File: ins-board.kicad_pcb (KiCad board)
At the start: 4 copper layers, 50 x 23 mm, 93 parts, among them P1 POWER, Q1 FDN306P, Q2 FDC638APZ, U1 24LC128, U10 HMC5883L, U11 H3LIS331DL, U2 STM32F415RGT6, U3 LTC4412, U4 MAX3051, U5 LT1965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

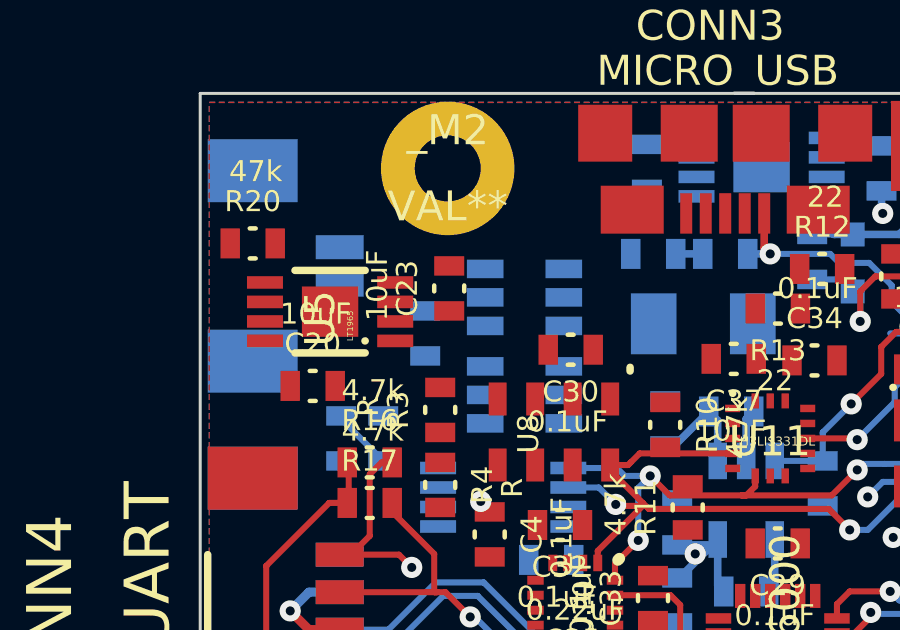
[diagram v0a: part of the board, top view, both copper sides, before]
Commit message: solid copper connection for mounting holes
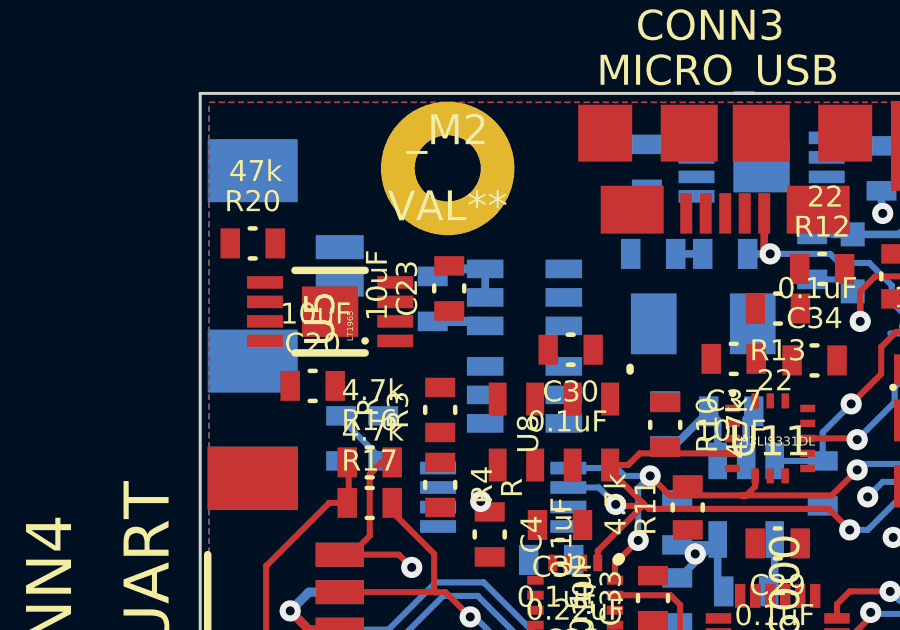
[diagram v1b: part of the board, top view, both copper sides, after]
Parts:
- moved C17 1.18 mm to (39.8, 32.9)
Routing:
- net GND: track 56.4 -> 59.2 mm
- net /V_DC: track 0.00 -> 1.81 mm
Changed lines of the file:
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@@
   (general
     (links 269)
-    (no_connects 89)
+    (no_connects 87)
     (area 16.4 15.14 86.7782 50.939311)
     (thickness 1.6)
     (drawings 6)
-    (tracks 810)
+    (tracks 815)
     (zones 0)
     (modules 93)
@@
   )
   (setup
-    (last_trace_width 0.254)
+    (last_trace_width 0.3048)
     (user_trace_width 0.2032)
     (user_trace_width 0.254)
@@
       (layers *.Cu *.Mask F.SilkS)
       (net 52 GND)
+      (zone_connect 2)
     )
   )
@@
       (layers *.Cu *.Mask F.SilkS)
       (net 52 GND)
+      (zone_connect 2)
     )
   )
@@
       (layers *.Cu *.Mask F.SilkS)
       (net 52 GND)
+      (zone_connect 2)
     )
   )
@@
       (layers *.Cu *.Mask F.SilkS)
       (net 52 GND)
+      (zone_connect 2)
     )
   )
@@
   )
   (module _0603-W (layer B.Cu)
-    (at 39.5 34 90)
+    (at 39.75 32.85 90)
     (fp_text reference C17 (at 0 1.4 90) (layer B.SilkS)
       (effects (font (size 0.7 0.7) (thickness 0.15)) (justify mirror))
@@
   (segment (start 70 41.45) (end 70 41.2) (width 0.2032) (layer F.Cu) (net 17))
   (segment (start 70.55 42) (end 70 41.45) (width 0.2032) (layer F.Cu) (net 17))
-  (segment (start 52.4 32.2) (end 53.35 32.2) (width 0.2032) (layer B.Cu) (net 18) (status C00000))
-  (segment (start 53.35 32.2) (end 53.75 32.6) (width 0.2032) (layer B.Cu) (net 18) (status C00000))
+  (segment (start 52.4 32.2) (end 53.35 32.2) (width 0.2032) (layer B.Cu) (net 18))
+  (segment (start 53.35 32.2) (end 53.75 32.6) (width 0.2032) (layer B.Cu) (net 18))
   (segment (start 54 33.6) (end 54 32.85) (width 0.2032) (layer B.Cu) (net 18))
   (via (at 54 33.6) (size 0.706) (layers F.Cu B.Cu) (net 18))
@@
   (segment (start 60.9 38.95) (end 55.3 38.95) (width 0.2032) (layer B.Cu) (net 48))
   (segment (start 55.3 38.95) (end 55.25 38.95) (width 0.2032) (layer B.Cu) (net 48))
+  (segment (start 39.75 33.6) (end 41.35 33.6) (width 0.3048) (layer B.Cu) (net 49) (status C00000))
+  (segment (start 41.35 33.6) (end 41.5 33.75) (width 0.3048) (layer B.Cu) (net 49) (status C00000))
   (segment (start 51 31.35) (end 53 31.35) (width 0.2032) (layer B.Cu) (net 51))
   (segment (start 56.525 33.275) (end 56.25 33.55) (width 0.2032) (layer B.Cu) (net 51))
@@
   (segment (start 66.25 38.75) (end 66 39) (width 0.2032) (layer F.Cu) (net 51))
   (segment (start 66.25 38.75) (end 66 39) (width 0.2032) (layer F.Cu) (net 51))
+  (segment (start 41.5 31.85) (end 40 31.85) (width 0.3048) (layer B.Cu) (net 52) (status C00000))
+  (segment (start 40 31.85) (end 39.75 32.1) (width 0.3048) (layer B.Cu) (net 52) (status C00000))
+  (segment (start 41.5 31.85) (end 41.5 32.8) (width 0.254) (layer B.Cu) (net 52))
   (segment (start 54.7116 29.2488) (end 54.7116 29.9616) (width 0.254) (layer B.Cu) (net 52))
   (via (at 54.75 30) (size 0.706) (layers F.Cu B.Cu) (net 52))
@@
   (segment (start 58.55 47.9) (end 58.5 47.9) (width 0.2032) (layer B.Cu) (net 69))
   (segment (start 62.65 45.2) (end 62 45.85) (width 0.2032) (layer B.Cu) (net 69))
-  (segment (start 56.05 31.65) (end 56.05 31.1) (width 0.2032) (layer B.Cu) (net 70) (status 400000))
+  (segment (start 56.05 31.65) (end 56.05 31.1) (width 0.2032) (layer B.Cu) (net 70))
   (via (at 56.1 31.05) (size 0.706) (layers F.Cu B.Cu) (net 70))
   (segment (start 56.05 31.1) (end 56.1 31.05) (width 0.2032) (layer B.Cu) (net 70))
@@
   (segment (start 36.7 36.75) (end 36.7 36.85) (width 0.2032) (layer B.Cu) (net 76))
   (segment (start 36.7 36.85) (end 38.1 38.25) (width 0.2032) (layer B.Cu) (net 76))
-  (segment (start 53.15 30.7) (end 52.4 30.7) (width 0.2032) (layer B.Cu) (net 77) (status 800000))
+  (segment (start 53.15 30.7) (end 52.4 30.7) (width 0.2032) (layer B.Cu) (net 77))
   (segment (start 53.1 30.7) (end 53.15 30.7) (width 0.254) (layer B.Cu) (net 77))
   (segment (start 53.15 30.7) (end 55.3 30.7) (width 0.254) (layer B.Cu) (net 77))

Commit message: power routing
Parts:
- moved R13 2.04 mm to (49.4, 32.5), turned to 90 degrees
- moved C5 1.70 mm to (56.5, 42.6), turned to 90 degrees
- moved R12 1.44 mm to (51.6, 32.8)
- moved C26 0.78 mm to (48.1, 34.1)
- moved C9 0.57 mm to (57.8, 42.6), turned to 90 degrees
- moved R8 0.07 mm to (72.1, 38.9)
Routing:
- net /VCC_IO: track 10.4 -> 93.0 mm, vias 0 -> 5
- net /V_IN: track 0.00 -> 16.7 mm
- net VCC: track 37.5 -> 53.7 mm
- net /USB_DP: track 15.8 -> 24.6 mm, vias 1 -> 2
- net /Sensors/I2C_SDA: track 27.8 -> 32.1 mm, vias 4 -> 5
- net /USB_DM: track 19.1 -> 22.3 mm, vias 1 -> 2
- net N-0000043: track 0.00 -> 3.04 mm
- net GND: track 59.2 -> 61.5 mm
- net N-0000044: track 0.00 -> 1.76 mm
- net (no net): track 0.00 -> 0.94 mm, vias 0 -> 1

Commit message: power routing
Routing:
- net VCC: track 53.7 -> 77.8 mm, vias 7 -> 9
- net /VCC_IO: track 93.0 -> 94.9 mm
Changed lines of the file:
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@@
   (general
     (links 269)
-    (no_connects 65)
+    (no_connects 64)
     (area 16.4 15.14 86.7782 50.939311)
     (thickness 1.6)
     (drawings 6)
-    (tracks 919)
+    (tracks 934)
     (zones 0)
     (modules 93)
@@
   )
   (setup
-    (last_trace_width 0.3556)
+    (last_trace_width 0.508)
     (user_trace_width 0.2032)
     (user_trace_width 0.254)
@@
   (segment (start 55.2 34.4) (end 54.9 34.4) (width 0.2032) (layer B.Cu) (net 46))
   (segment (start 49.9 33.75) (end 49.35 33.2) (width 0.2032) (layer F.Cu) (net 46))
+  (segment (start 40.3 33.25) (end 39.95 33.6) (width 0.508) (layer F.Cu) (net 47) (status 400000))
+  (segment (start 39.95 33.6) (end 38.5 33.6) (width 0.508) (layer F.Cu) (net 47) (status 800000))
   (segment (start 36.65 45.125) (end 35.075 45.125) (width 0.508) (layer F.Cu) (net 47))
   (segment (start 34.1 41.9) (end 34.9 41.1) (width 0.508) (layer F.Cu) (net 47))
@@
   (segment (start 58.55 47.9) (end 58.5 47.9) (width 0.2032) (layer B.Cu) (net 69))
   (segment (start 62.65 45.2) (end 62 45.85) (width 0.2032) (layer B.Cu) (net 69))
+  (segment (start 57.95 30) (end 57.95 30.9) (width 0.254) (layer B.Cu) (net 70))
+  (segment (start 57.5 31.35) (end 56.8 31.35) (width 0.254) (layer F.Cu) (net 70) (status 800000))
+  (via (at 57.5 31.35) (size 0.706) (layers F.Cu B.Cu) (net 70))
+  (segment (start 57.95 30.9) (end 57.5 31.35) (width 0.254) (layer B.Cu) (net 70))
+  (segment (start 57.95 30) (end 57.95 29.25) (width 0.254) (layer B.Cu) (net 70))
   (segment (start 56.05 31.65) (end 56.05 31.1) (width 0.2032) (layer B.Cu) (net 70))
   (via (at 56.1 31.05) (size 0.706) (layers F.Cu B.Cu) (net 70))
   (segment (start 56.05 31.1) (end 56.1 31.05) (width 0.2032) (layer B.Cu) (net 70))
-  (segment (start 57.2 30) (end 57.2 30.35) (width 0.254) (layer B.Cu) (net 70))
-  (segment (start 56.8 31.35) (end 56.8 30.8) (width 0.3048) (layer F.Cu) (net 70))
-  (segment (start 57 30.6) (end 56.8 30.8) (width 0.3048) (layer F.Cu) (net 70))
   (segment (start 63.2 29.4) (end 62.9 29.1) (width 0.254) (layer B.Cu) (net 70))
-  (segment (start 62.9 29.1) (end 58.1 29.1) (width 0.254) (layer B.Cu) (net 70))
-  (segment (start 58.1 29.1) (end 57.2 30) (width 0.254) (layer B.Cu) (net 70))
   (segment (start 63.2 29.4) (end 63.2 30.4) (width 0.254) (layer B.Cu) (net 70))
-  (segment (start 57 30.55) (end 57 30.6) (width 0.254) (layer F.Cu) (net 70))
-  (segment (start 57.05 30.5) (end 57 30.55) (width 0.254) (layer F.Cu) (net 70))
-  (via (at 57.05 30.5) (size 0.706) (layers F.Cu B.Cu) (net 70))
-  (segment (start 57.2 30.35) (end 57.05 30.5) (width 0.254) (layer B.Cu) (net 70))
+  (segment (start 58.1 29.1) (end 57.95 29.25) (width 0.254) (layer B.Cu) (net 70))
+  (segment (start 62.9 29.1) (end 58.1 29.1) (width 0.254) (layer B.Cu) (net 70))
   (segment (start 56.8 31.35) (end 55.2 31.35) (width 0.3048) (layer F.Cu) (net 70))
   (segment (start 48.2 44.8) (end 49.1 44.8) (width 0.2032) (layer B.Cu) (net 74))
@@
   (segment (start 36.7 36.75) (end 36.7 36.85) (width 0.2032) (layer B.Cu) (net 76))
   (segment (start 36.7 36.85) (end 38.1 38.25) (width 0.2032) (layer B.Cu) (net 76))
+  (segment (start 38.9 36.7) (end 40.45 35.15) (width 0.2032) (layer Inner2.Cu) (net 77))
+  (segment (start 54.95 28.85) (end 56.05 29.95) (width 0.2032) (layer Inner2.Cu) (net 77))
+  (segment (start 54.05 28.85) (end 54.95 28.85) (width 0.2032) (layer Inner2.Cu) (net 77))
+  (segment (start 53.4 29.5) (end 54.05 28.85) (width 0.2032) (layer Inner2.Cu) (net 77))
+  (segment (start 44.95 29.5) (end 53.4 29.5) (width 0.2032) (layer Inner2.Cu) (net 77))
+  (segment (start 40.45 34) (end 44.95 29.5) (width 0.2032) (layer Inner2.Cu) (net 77))
+  (segment (start 40.45 35.15) (end 40.45 34) (width 0.2032) (layer Inner2.Cu) (net 77))
+  (segment (start 38.1 36.75) (end 38.85 36.75) (width 0.2032) (layer B.Cu) (net 77) (status 400000))
+  (segment (start 38.9 36.7) (end 38.9 36.75) (width 0.2032) (layer F.Cu) (net 77))
+  (via (at 38.9 36.7) (size 0.706) (layers F.Cu B.Cu) (net 77))
+  (segment (start 38.85 36.75) (end 38.9 36.7) (width 0.2032) (layer B.Cu) (net 77))
+  (segment (start 56.05 28.65) (end 56.05 29) (width 0.508) (layer B.Cu) (net 77))
+  (via (at 57 29.95) (size 0.706) (layers F.Cu B.Cu) (net 77))
+  (segment (start 56.05 29) (end 57 29.95) (width 0.508) (layer B.Cu) (net 77))
   (segment (start 52.8828 28.1328) (end 54.3276 28.1328) (width 0.3556) (layer B.Cu) (net 77) (status 400000))
   (segment (start 54.3276 28.1328) (end 54.7116 27.7488) (width 0.3556) (layer B.Cu) (net 77) (status 800000))
@@
   (segment (start 54.7116 27.7488) (end 55.4988 27.7488) (width 0.508) (layer B.Cu) (net 77))
   (segment (start 55.4988 27.7488) (end 56.05 28.3) (width 0.508) (layer B.Cu) (net 77))
-  (segment (start 56.05 28.3) (end 56.05 29.95) (width 0.508) (layer B.Cu) (net 77))
+  (segment (start 56.05 28.3) (end 56.05 28.65) (width 0.508) (layer B.Cu) (net 77))
+  (segment (start 56.05 28.65) (end 56.05 29.95) (width 0.508) (layer B.Cu) (net 77))
   (segment (start 73.3 31.85) (end 73.9 32.45) (width 0.2032) (layer F.Cu) (net 77))
   (via (at 74.25 32.45) (size 0.706) (layers F.Cu B.Cu) (net 77))
@@
   (via (at 60.6 34.9) (size 0.706) (layers F.Cu B.Cu) (net 77))
   (segment (start 56.05 29.95) (end 56.3 29.7) (width 0.2032) (layer F.Cu) (net 77))
-  (via (at 56.05 29.95) (size 0.706) (layers F.Cu B.Cu) (net 77))
-  (segment (start 58.625 30.225) (end 58.625 30.65) (width 0.2032) (layer F.Cu) (net 77))
-  (segment (start 58.1 29.7) (end 58.625 30.225) (width 0.2032) (layer F.Cu) (net 77))
   (segment (start 56.3 29.7) (end 58.1 29.7) (width 0.2032) (layer F.Cu) (net 77))
+  (segment (start 58.1 29.7) (end 58.625 30.225) (width 0.2032) (layer F.Cu) (net 77))
+  (segment (start 58.625 30.225) (end 58.625 30.65) (width 0.2032) (layer F.Cu) (net 77))
+  (via (at 56.05 29.95) (size 0.706) (layers F.Cu B.Cu) (net 77))
   (segment (start 56.5 43.4) (end 57.1 44) (width 0.254) (layer F.Cu) (net 77))
   (via (at 57.1 44.55) (size 0.706) (layers F.Cu B.Cu) (net 77))
@@
   (segment (start 53.1 30.7) (end 53.15 30.7) (width 0.254) (layer B.Cu) (net 77))
   (segment (start 53.15 30.7) (end 55.3 30.7) (width 0.254) (layer B.Cu) (net 77))
+  (segment (start 55.3 30.7) (end 56.05 29.95) (width 0.254) (layer B.Cu) (net 77))
   (segment (start 55.4988 27.7488) (end 56.05 28.3) (width 0.3048) (layer B.Cu) (net 77))
   (segment (start 56.05 28.3) (end 56.05 29.95) (width 0.3048) (layer B.Cu) (net 77))
-  (segment (start 55.3 30.7) (end 56.05 29.95) (width 0.254) (layer B.Cu) (net 77))
   (segment (start 63.8 47.35) (end 64.5 48.05) (width 0.2032) (layer B.Cu) (net 77))
   (segment (start 64.5 48.05) (end 66.65 48.05) (width 0.2032) (layer B.Cu) (net 77))

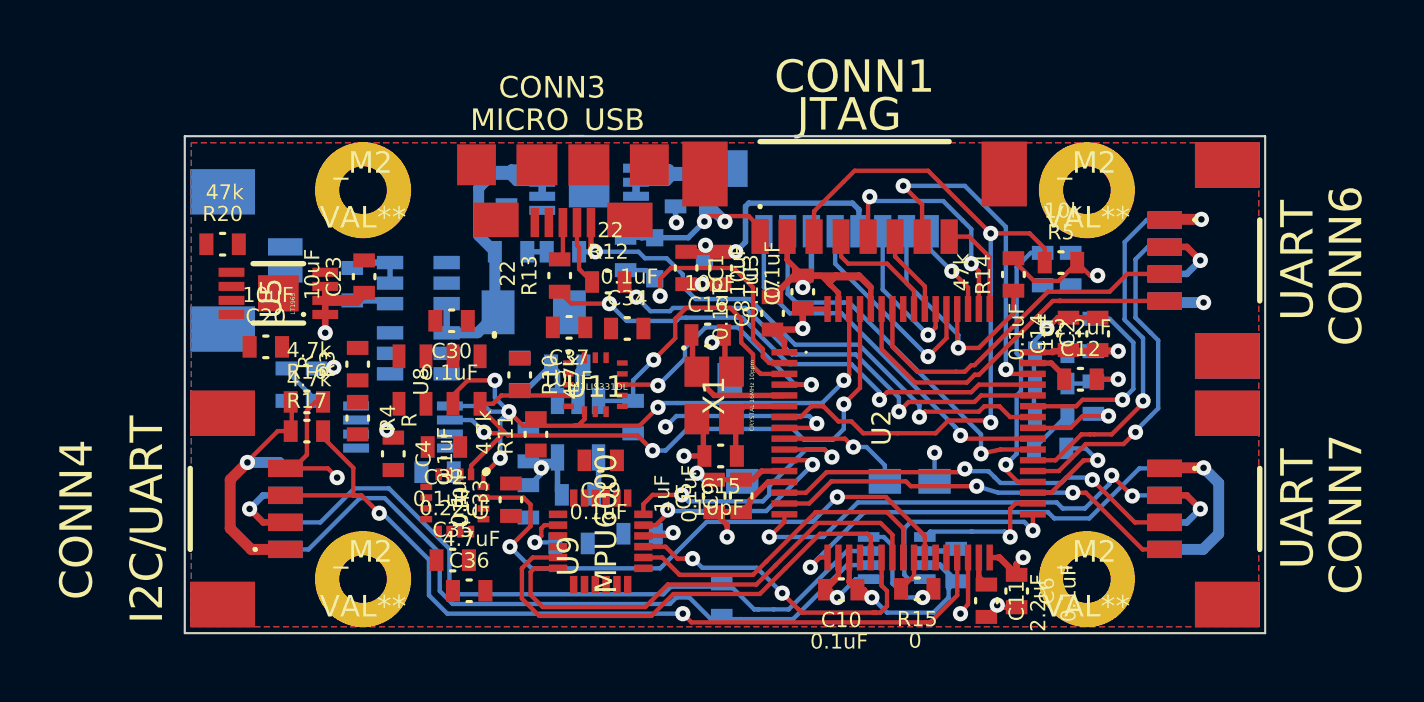
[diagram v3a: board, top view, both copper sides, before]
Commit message: routing, added dimensions
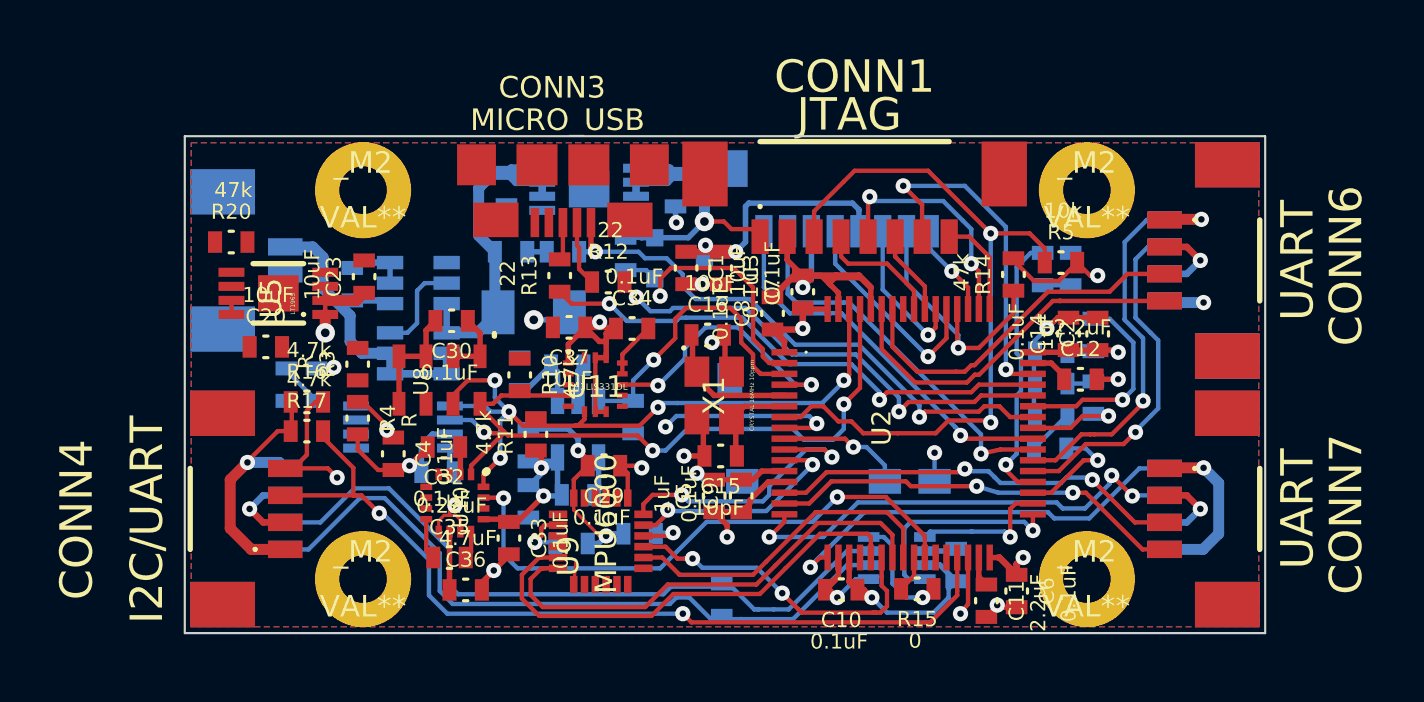
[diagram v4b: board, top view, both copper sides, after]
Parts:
- moved C33 1.78 mm to (47.0, 44.6), turned to 270 degrees
- moved R20 0.41 mm to (34.1, 30.9)
- moved C29 0.29 mm to (51.4, 41.2)
- moved C34 0.22 mm to (52.7, 34.9)
- moved C35 0.19 mm to (44.2, 45.5)
- moved C36 0.17 mm to (45.0, 47.0)
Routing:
- net GND: track 61.5 -> 95.4 mm, vias 13 -> 19
- net /Sensors/VCC_A: track 5.82 -> 30.1 mm, vias 1 -> 4
- net /V_DC: track 1.81 -> 15.4 mm
- net N-0000051: track 0.00 -> 4.45 mm
- net VCC: track 77.8 -> 75.1 mm, vias 9 -> 8
- net N-0000082: track 0.00 -> 2.70 mm
- net /V_BAT_MON_AD: track 36.6 -> 39.0 mm
- net N-0000081: track 0.00 -> 1.91 mm
- net N-0000083: track 0.00 -> 1.30 mm
- net N-0000052: track 0.00 -> 1.30 mm
- net /Sensors/HMC5883L_DRDY: track 27.4 -> 26.4 mm

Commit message: routing (io_en)
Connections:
- U2 pad 28: /IO_EN -> (no net)
- U2 pad 57: (no net) -> /IO_EN
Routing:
- net /IO_EN: track 0.00 -> 46.9 mm, vias 0 -> 2
- net GND: track 95.4 -> 92.6 mm
- net /V_IN: track 16.7 -> 19.2 mm
- net /SDIO_D3: track 12.5 -> 9.98 mm
- net /STM32F4_TMS: track 16.2 -> 15.3 mm
- net /STM32F4_NRST: track 34.2 -> 35.1 mm
